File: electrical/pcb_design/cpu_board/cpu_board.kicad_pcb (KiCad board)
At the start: 2 copper layers, 90 x 90 mm, 36 parts, among them J3 Conn_01x15_Pin, J4 Conn_01x15_Pin, U1 STM32F103C8T6, U2 AMS1117-3.3, Y1 16MHz

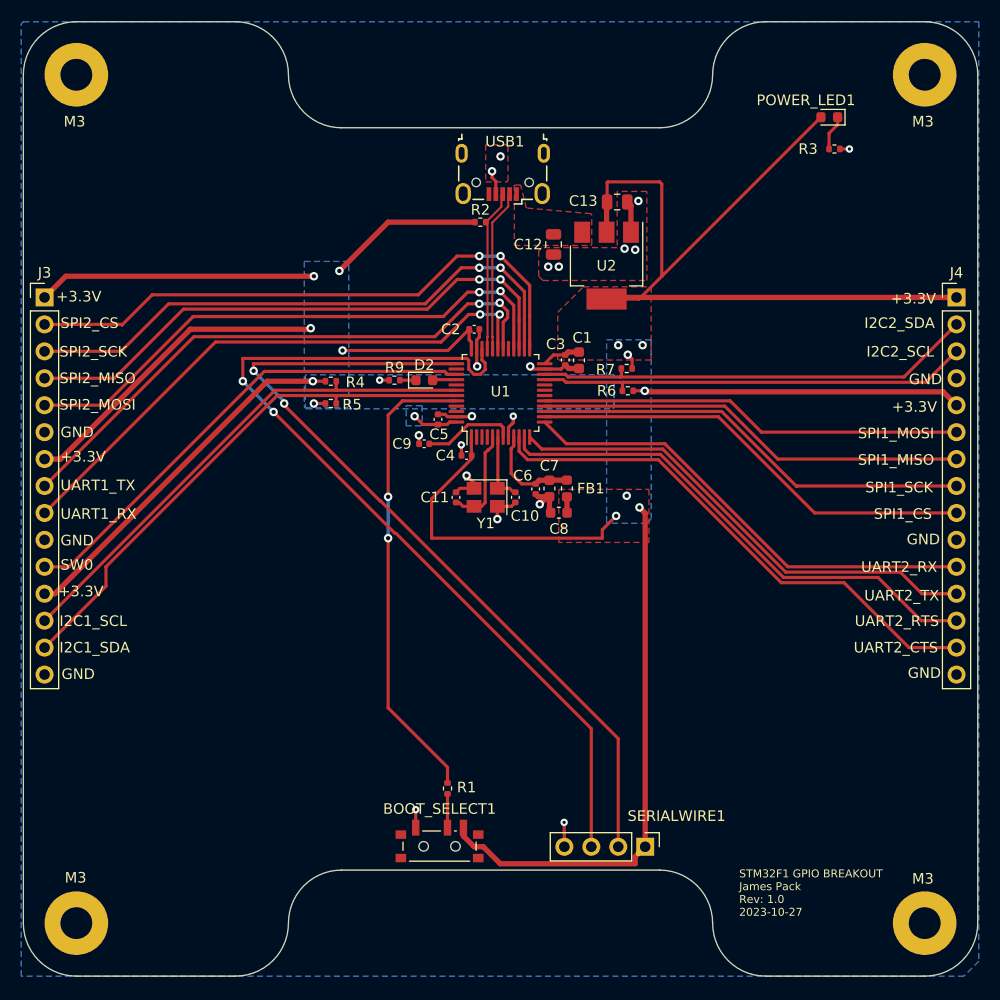
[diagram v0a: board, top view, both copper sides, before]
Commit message: Fixed multiple small issues with design, including switching USB receptacles, adding proper debug headers, and changing out the BOOT0 switch for a simple jumper configuration.
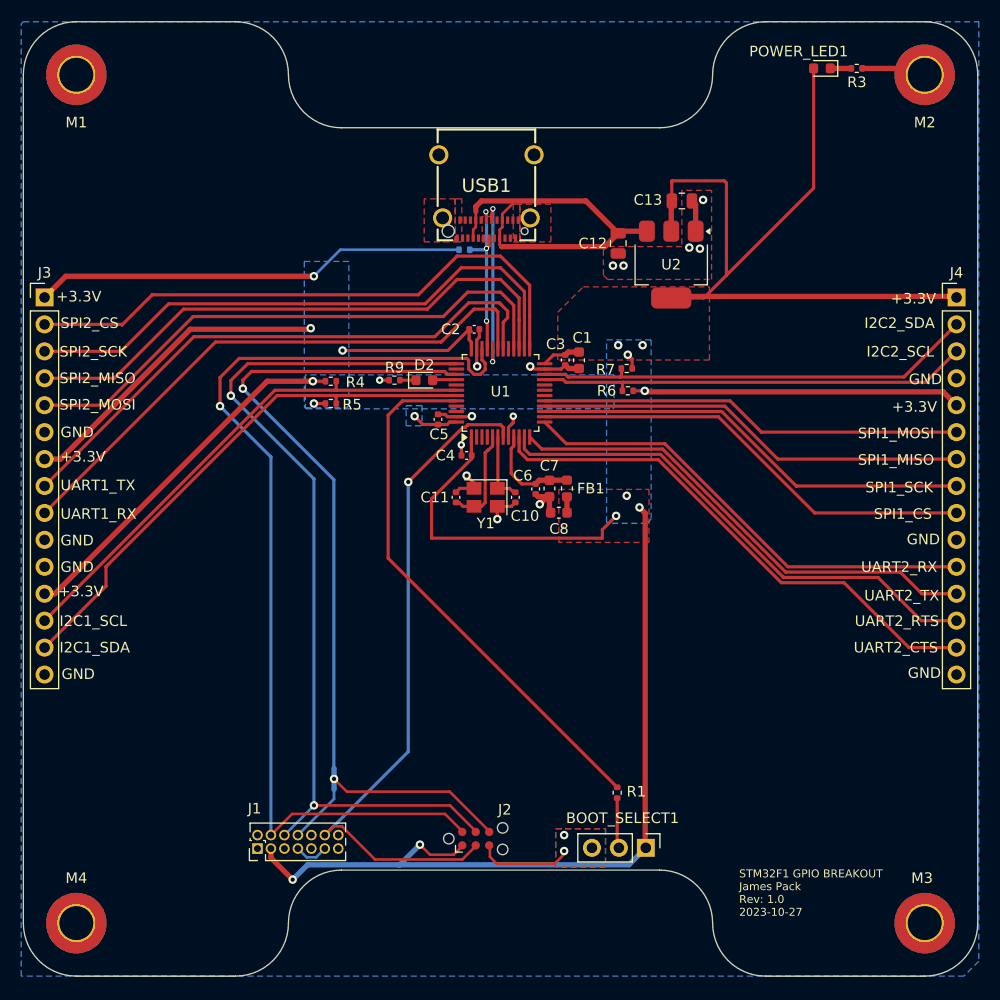
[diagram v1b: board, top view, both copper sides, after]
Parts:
- removed C9: 100n, Capacitor_SMD:C_0402_1005Metric
- removed H1, H2, H3, H4: MountingHole, MountingHole:MountingHole_3mm_Pad
- removed SERIALWIRE1: Conn_01x04_Pin, Connector_PinHeader_2.54mm:PinHeader_1x04_P2.54mm_Vertical
- added J1: STLINK_STDC14, Connector_PinHeader_1.27mm:PinHeader_2x07_P1.27mm_Vertical, F.Cu at (122.1, 138.0)
- added J2: STLINK_TagConnect_6, Connector:Tag-Connect_TC2030-IDC-NL_2x03_P1.27mm_Vertical, F.Cu at (142.7, 137.0)
- added M1: M3, MountingHole:MountingHole_3.2mm_M3_ISO7380_Pad_TopBottom, F.Cu at (105.0, 65.0)
- added M2: M3, MountingHole:MountingHole_3.2mm_M3_ISO7380_Pad_TopBottom, F.Cu at (185.0, 65.0)
- added M3: M3, MountingHole:MountingHole_3.2mm_M3_ISO7380_Pad_TopBottom, F.Cu at (185.0, 145.0)
- added M4: M3, MountingHole:MountingHole_3.2mm_M3_ISO7380_Pad_TopBottom, F.Cu at (105.0, 145.0)
- added NT1: SWO_Tie, NetTie:NetTie-3_SMD_Pad0.5mm, B.Cu at (129.3, 131.4)
- BOOT_SELECT1: value SW_SPDT -> Conn_01x03_Pin; footprint Button_Switch_SMD:SW_SPDT_PCM12 -> Connector_PinHeader_2.54mm:PinHeader_1x03_P2.54mm_Vertical
- R2: moved to B.Cu
- USB1: value USB_B_Micro -> USB_C_Receptacle_Power_Only; footprint Connector_USB:USB_Micro-B_Wuerth_629105150521 -> footprints:12401832E402A
- moved BOOT_SELECT1 19.5 mm to (158.7, 137.9), turned to -90 degrees
- moved R1 16.0 mm to (156.0, 132.7)
- moved R3 7.88 mm to (178.6, 64.4)
- moved C12 6.10 mm to (156.1, 80.9)
- moved C13 6.10 mm to (162.1, 76.9)
- moved U2 6.10 mm to (161.1, 82.9)
- moved POWER_LED1 4.65 mm to (175.3, 64.4)
- moved R2 3.01 mm to (141.6, 81.5)
- moved USB1 1.85 mm to (143.7, 75.4)
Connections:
- BOOT_SELECT1 pad 1: GND -> +3.3V
- BOOT_SELECT1 pad 3: +3.3V -> GND
- J3 pad 11: SW0 -> GND
- U1 pad 7: /NRST -> NRST
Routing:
- net NRST: track 0.00 -> 65.3 mm, vias 0 -> 1
- net VBUS: track 0.83 -> 37.7 mm
- net +3.3V: track 325.5 -> 347.2 mm, vias 14 -> 15
- net Net-(J2-T_SWO): track 0.00 -> 16.8 mm, vias 0 -> 1
- net SW0: track 46.6 -> 60.8 mm, vias 0 -> 1
- net GND: track 37.4 -> 48.0 mm, vias 20 -> 16
- net /NRST: track 8.73 -> 0.00 mm
- net SWDIO: track 86.0 -> 93.9 mm, vias 2 -> 1
- net /BOOT0: track 44.0 -> 51.0 mm, vias 2 -> 0
- net SWCLK: track 79.0 -> 85.6 mm
- net Net-(J1-T_SWO): track 0.00 -> 5.71 mm
- net USB_D-: track 15.3 -> 16.9 mm, vias 0 -> 2
- net /sw_boot0: track 3.19 -> 4.76 mm
- net /PWR_LED_K: track 3.33 -> 1.98 mm
- net USB_D+: track 15.2 -> 16.5 mm, vias 0 -> 3
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- added copper zone on F.Cu, net USB_D-
- removed copper zone on F.Cu, net VBUS
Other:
- board text removed: "M3"
- board text removed: "SW0"

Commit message: Fixed several minor issues in preparation of manufacturing the CPU board
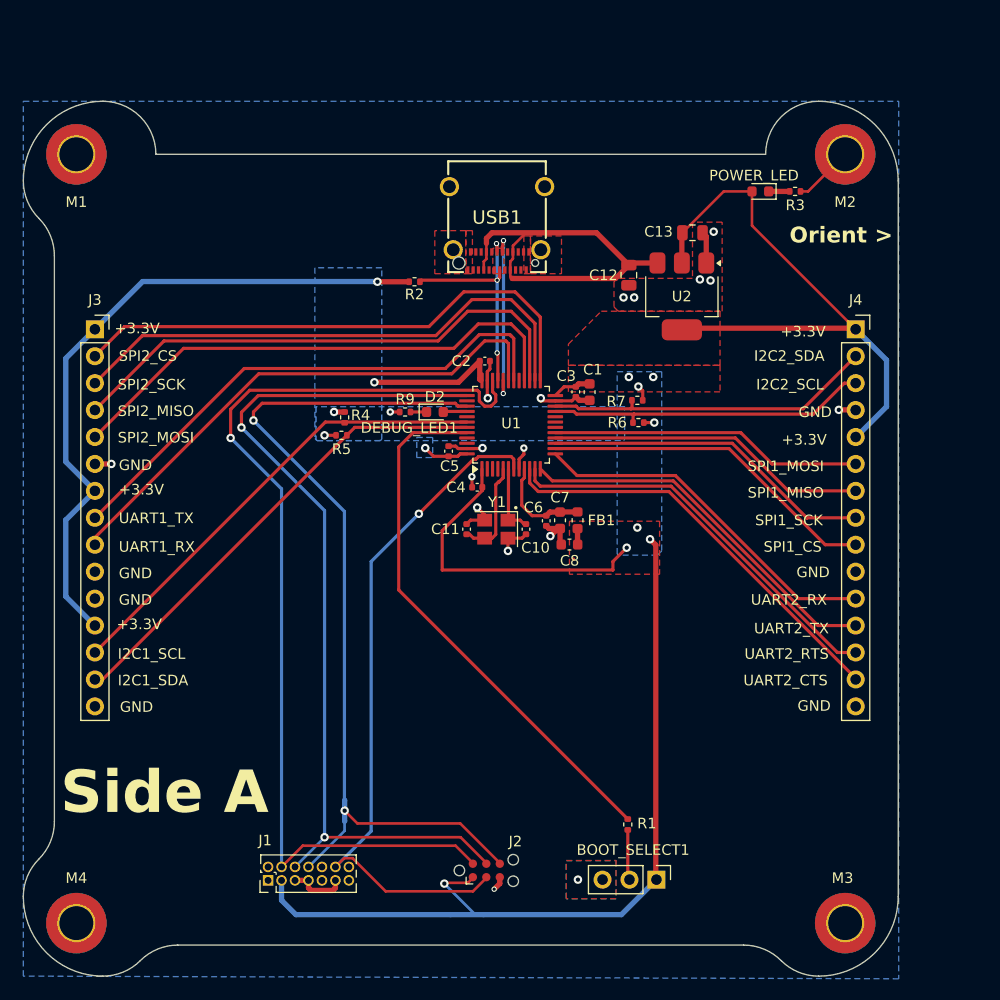
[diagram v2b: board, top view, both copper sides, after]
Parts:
- D2: value BLUE -> DEBUG_LED1
- J3, J4: footprint Connector_PinHeader_2.54mm:PinHeader_1x15_P2.54mm_Vertical -> Connector_PinSocket_2.54mm:PinSocket_1x15_P2.54mm_Vertical
- POWER_LED1: value GREEN -> POWER_LED
- R2: moved to F.Cu
- moved POWER_LED1 13.0 mm to (169.5, 76.0)
- moved R3 13.0 mm to (172.8, 76.0)
- moved M2 10.6 mm to (177.5, 72.5)
- moved J4 9.97 mm to (178.5, 89.0)
- moved M1 7.50 mm to (105.0, 72.5)
- moved M3 7.50 mm to (177.5, 145.0)
- moved J3 5.62 mm to (106.8, 89.0)
- moved R2 5.59 mm to (136.9, 84.5)
- moved R4 3.65 mm to (130.3, 97.3), turned to -90 degrees
- moved BOOT_SELECT1 3.16 mm to (159.7, 140.9)
- moved C1 3.16 mm to (153.4, 94.9)
- moved C10 3.16 mm to (147.4, 107.8)
- moved C11 3.16 mm to (141.8, 107.8)
- moved C12 3.16 mm to (157.1, 83.9)
- moved C13 3.16 mm to (163.1, 79.9)
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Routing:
- net +3.3V: track 347.2 -> 258.1 mm, vias 15 -> 13
- net UART2_RTS: track 48.6 -> 38.1 mm
- net SPI1_SCK: track 41.8 -> 31.3 mm
- net UART2_RX: track 44.5 -> 34.0 mm
- net SPI1_MOSI: track 40.1 -> 29.5 mm
- net SPI1_MISO: track 40.9 -> 30.4 mm
- net SPI1_CS: track 42.6 -> 32.1 mm
- net I2C2_SCL: track 41.0 -> 30.5 mm
- net I2C2_SDA: track 41.8 -> 31.3 mm
- net UART2_TX: track 46.4 -> 35.9 mm
- net UART2_CTS: track 50.3 -> 39.8 mm
- net USB_D+: track 16.5 -> 22.2 mm
- net I2C1_SDA: track 50.4 -> 44.8 mm
- net I2C1_SCL: track 48.7 -> 44.1 mm
- net SPI2_CS: track 55.6 -> 51.5 mm
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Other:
- board size 90 x 90 mm -> 82.5 x 82.5 mm
- board text added: "Orient >"
- board text added: "Side A"
- board text added: "Side B"
- board text removed: "STM32F1 GPIO BREAKOUT James Pack Rev: 1.0 2023-10-27"

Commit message: Added CAN bus, tweaked other exposed signals
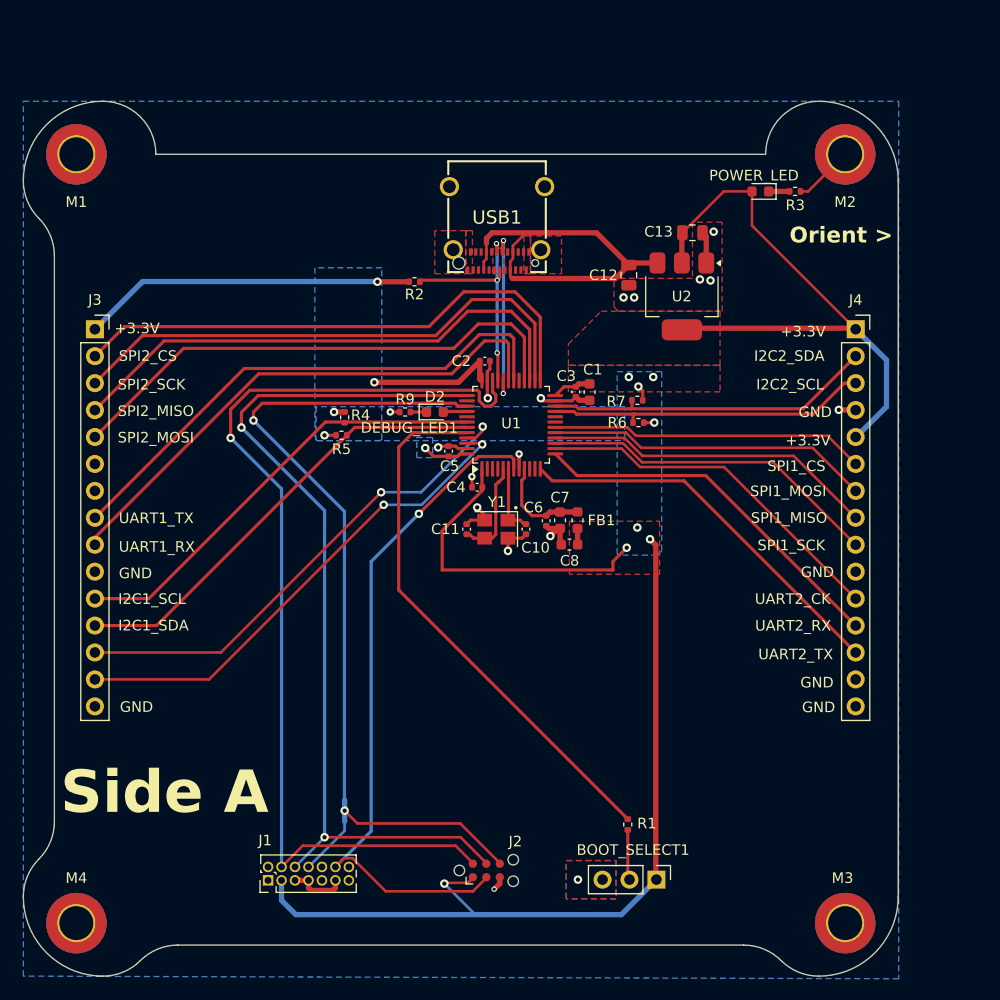
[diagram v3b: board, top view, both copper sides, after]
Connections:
- J3 pad 11: GND -> I2C1_SCL
- J3 pad 12: +3.3V -> I2C1_SDA
- J3 pad 13: I2C1_SCL -> CAN_RX
- J3 pad 14: I2C1_SDA -> CAN_TX
- J3 pad 6: GND -> unconnected-(J3-Pin_6-Pad6)
- J3 pad 7: +3.3V -> unconnected-(J3-Pin_7-Pad7)
- J4 pad 11: UART2_RX -> UART2_CK
- J4 pad 12: UART2_TX -> UART2_RX
- J4 pad 13: UART2_RTS -> UART2_TX
- J4 pad 14: UART2_CTS -> GND
- J4 pad 6: SPI1_MOSI -> SPI1_CS
- J4 pad 7: SPI1_MISO -> SPI1_MOSI
- J4 pad 8: SPI1_SCK -> SPI1_MISO
- J4 pad 9: SPI1_CS -> SPI1_SCK
- U1 pad 10: UART2_CTS -> unconnected-(U1-PA0-Pad10)
- U1 pad 11: UART2_RTS -> unconnected-(U1-PA1-Pad11)
- U1 pad 14: SPI1_CS -> UART2_CK
- U1 pad 18: unconnected-(U1-PB0-Pad18) -> SPI1_CS
- U1 pad 45: unconnected-(U1-PB8-Pad45) -> CAN_RX
- U1 pad 46: unconnected-(U1-PB9-Pad46) -> CAN_TX
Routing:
- net CAN_RX: track 0.00 -> 47.8 mm, vias 0 -> 2
- net CAN_TX: track 0.00 -> 47.2 mm, vias 0 -> 2
- net UART2_CTS: track 39.8 -> 0.00 mm
- net UART2_RTS: track 38.1 -> 0.00 mm
- net UART2_CK: track 0.00 -> 34.2 mm
- net +3.3V: track 258.1 -> 225.5 mm
- net GND: track 45.2 -> 42.8 mm, vias 18 -> 17
- net SPI1_CS: track 32.1 -> 29.8 mm
- net I2C1_SDA: track 44.8 -> 42.7 mm
- net I2C1_SCL: track 44.1 -> 42.0 mm
- net UART2_TX: track 35.9 -> 36.9 mm
- net SPI1_MISO: track 30.4 -> 31.4 mm
- net SPI1_MOSI: track 29.5 -> 30.6 mm
- net UART2_RX: track 34.0 -> 35.0 mm
- net SPI1_SCK: track 31.3 -> 32.3 mm
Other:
- board text added: "UART2_CK"
- board text removed: "UART2_CTS"
- board text removed: "UART2_RTS"
